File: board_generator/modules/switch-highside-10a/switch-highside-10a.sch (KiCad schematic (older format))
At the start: 7 parts, among them J1 Screw_Terminal_01x01, Q1 NTR5103N, U1 AUIPS7111S, X1 interface, X2 interface

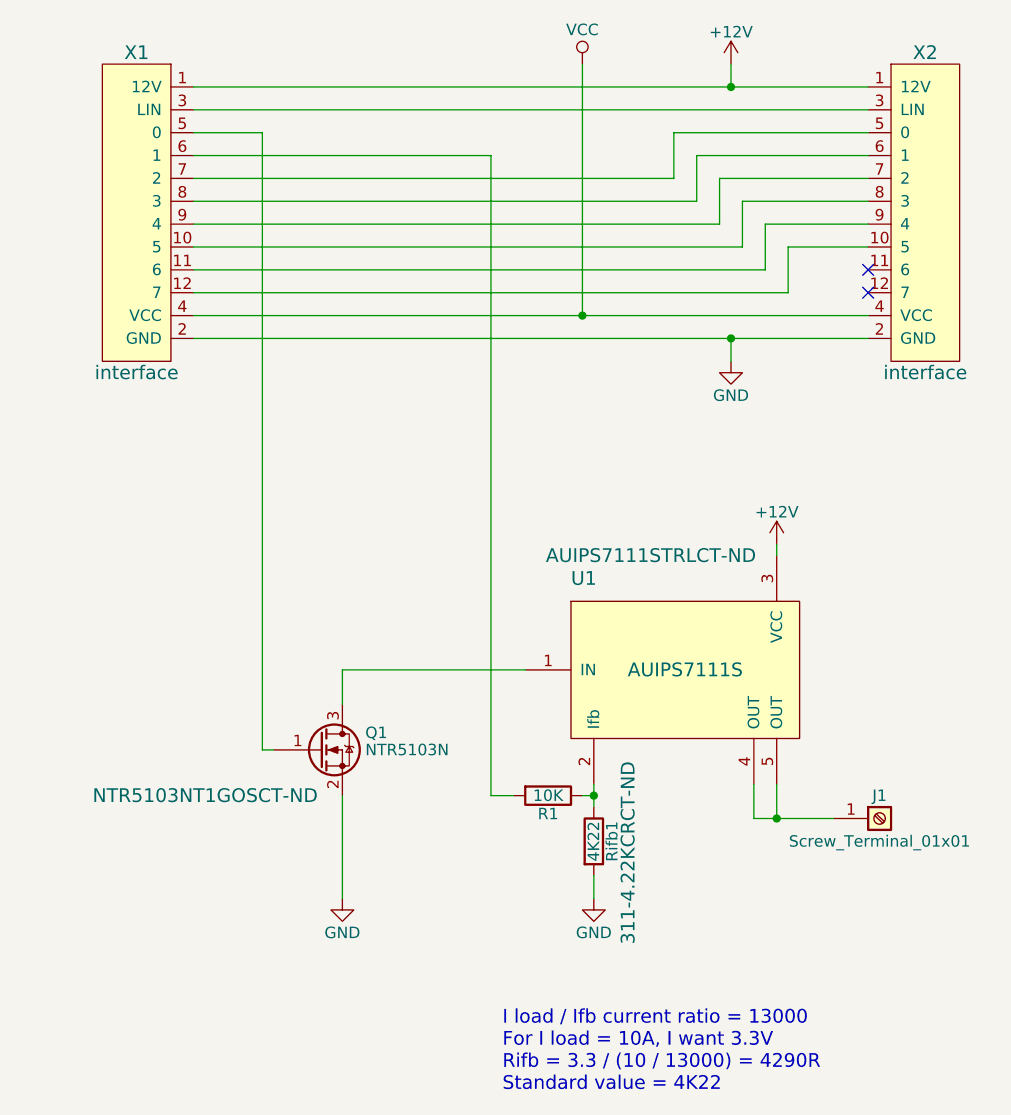
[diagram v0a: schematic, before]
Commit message: Adding pull-down on switch-highside-10a to disable output by default
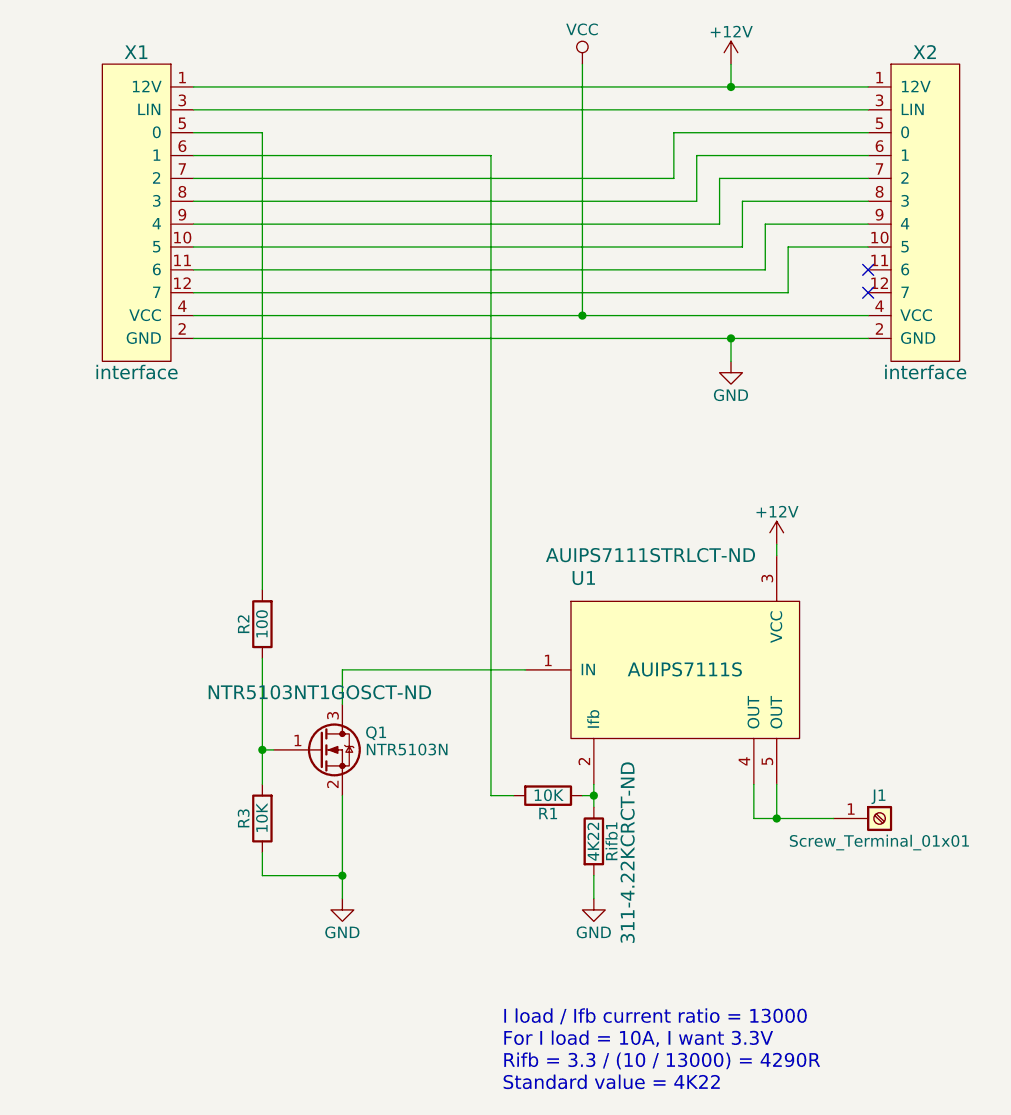
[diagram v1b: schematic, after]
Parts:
- added R2: 100, Resistors_SMD:R_0805_HandSoldering, symbol R
- added R3: 10K, Resistors_SMD:R_0805_HandSoldering, symbol R
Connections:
- net GND: now also R3.1
- net at X1.5 (0): now also R2.2; no longer Q1.1 (G)
- new net: Q1.1 (G), R2.1, R3.2
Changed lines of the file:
@@
 F 2 "TO_SOT_Packages_SMD:SOT-23" H 5200 4475 50  0001 L CIN
 F 3 "NTR5103N-D.PDF" H 5000 4550 50  0001 L CNN
-F 4 "NTR5103NT1GOSCT-ND" H 4500 4350 60  0000 C CNN "DIGIKEY"
+F 4 "NTR5103NT1GOSCT-ND" H 5000 4800 60  0000 C CNN "DIGIKEY"
 	1    5000 4550
 	1    0    0    -1
@@
 	4450 1850 4750 1850
 Wire Wire Line
-	4750 1850 4750 4550
-Wire Wire Line
 	4750 4550 4800 4550
 Text Notes 5800 6050 0    60   ~ 0
 I load / Ifb current ratio = 13000\nFor I load = 10A, I want 3.3V\nRifb = 3.3 / (10 / 13000) = 4290R\nStandard value = 4K22
+$Comp
+L R R3
+U 1 1 5A5EC140
+P 4750 4850
+F 0 "R3" V 4830 4850 50  0000 C CNN
+F 1 "10K" V 4750 4850 50  0000 C CNN
+F 2 "Resistors_SMD:R_0805_HandSoldering" V 4680 4850 50  0001 C CNN
+F 3 "" H 4750 4850 50  0001 C CNN
+F 4 "311-10.0KCRCT-ND" V 4750 4850 60  0001 C CNN "DIGIKEY"
+	1    4750 4850
+	-1   0    0    1
+$EndComp
+Connection ~ 4750 4550
+Wire Wire Line
+	4750 5000 4750 5100
+Wire Wire Line
+	4750 5100 5100 5100
+Connection ~ 5100 5100
+$Comp
+L R R2
+U 1 1 5A5EC27D
+P 4750 4000
+F 0 "R2" V 4830 4000 50  0000 C CNN
+F 1 "100" V 4750 4000 50  0000 C CNN
+F 2 "Resistors_SMD:R_0805_HandSoldering" V 4680 4000 50  0001 C CNN
+F 3 "" H 4750 4000 50  0001 C CNN
+F 4 "311-100CRCT-ND" V 4750 4000 60  0001 C CNN "DIGIKEY"
+	1    4750 4000
+	-1   0    0    1
+$EndComp
+Wire Wire Line
+	4750 4150 4750 4700
+Wire Wire Line
+	4750 1850 4750 3850
 $EndSCHEMATC

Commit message: Adding DigiKey references for switch-highside-10a
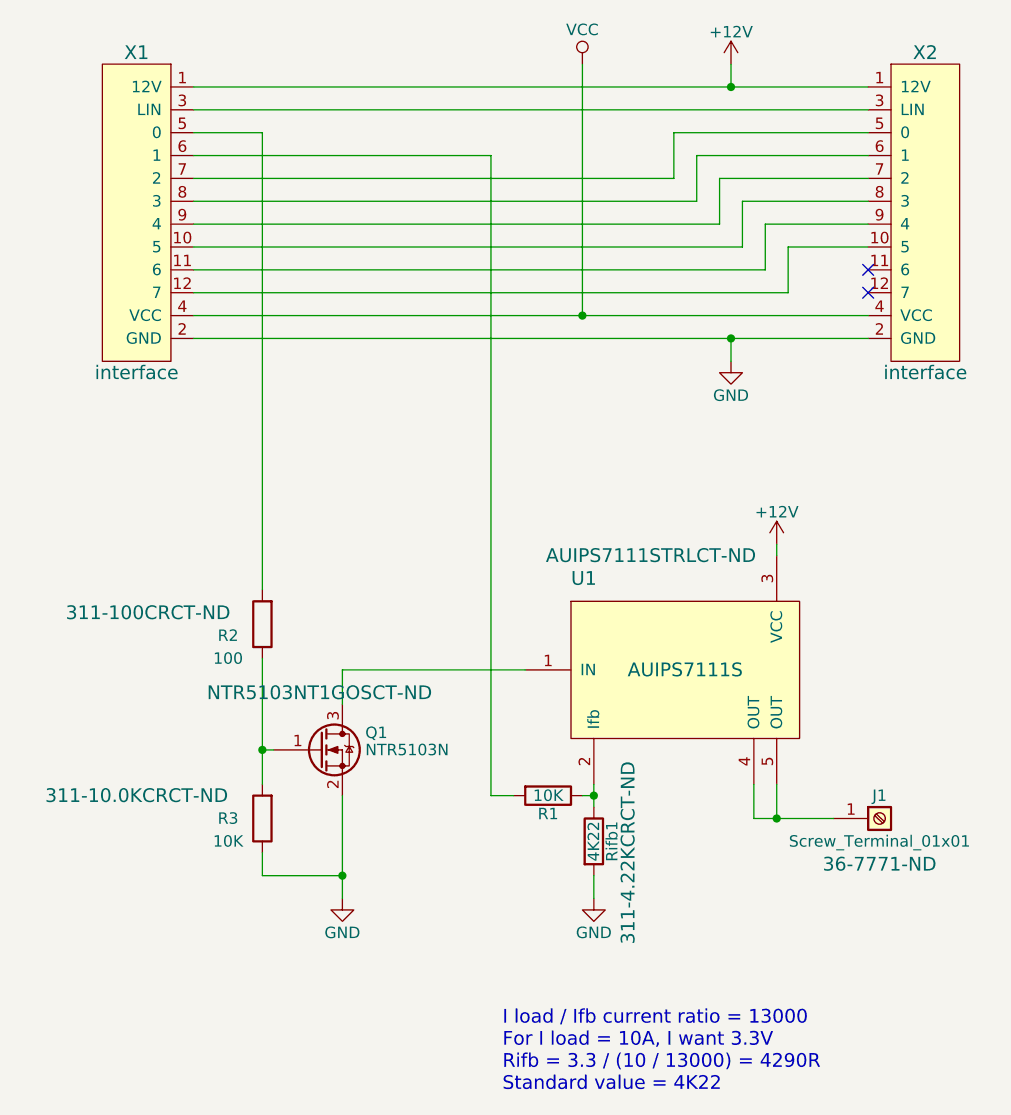
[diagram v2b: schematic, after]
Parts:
- J1: DIGIKEY (none) -> 36-7771-ND
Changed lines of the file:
@@
 F 2 "connectors:TERM_SCREW_M3" H 7450 4850 50  0001 C CNN
 F 3 "" H 7450 4850 50  0001 C CNN
+F 4 "36-7771-ND" H 7450 4650 60  0000 C CNN "DIGIKEY"
 	1    7450 4850
 	1    0    0    -1
@@
 U 1 1 5A5EC140
 P 4750 4850
-F 0 "R3" V 4830 4850 50  0000 C CNN
-F 1 "10K" V 4750 4850 50  0000 C CNN
+F 0 "R3" H 4900 4850 50  0000 C CNN
+F 1 "10K" H 4900 4950 50  0000 C CNN
 F 2 "Resistors_SMD:R_0805_HandSoldering" V 4680 4850 50  0001 C CNN
 F 3 "" H 4750 4850 50  0001 C CNN
-F 4 "311-10.0KCRCT-ND" V 4750 4850 60  0001 C CNN "DIGIKEY"
+F 4 "311-10.0KCRCT-ND" H 5300 4750 60  0000 C CNN "DIGIKEY"
 	1    4750 4850
 	-1   0    0    1
@@
 U 1 1 5A5EC27D
 P 4750 4000
-F 0 "R2" V 4830 4000 50  0000 C CNN
-F 1 "100" V 4750 4000 50  0000 C CNN
+F 0 "R2" H 4900 4050 50  0000 C CNN
+F 1 "100" H 4900 4150 50  0000 C CNN
 F 2 "Resistors_SMD:R_0805_HandSoldering" V 4680 4000 50  0001 C CNN
 F 3 "" H 4750 4000 50  0001 C CNN
-F 4 "311-100CRCT-ND" V 4750 4000 60  0001 C CNN "DIGIKEY"
+F 4 "311-100CRCT-ND" H 5250 3950 60  0000 C CNN "DIGIKEY"
 	1    4750 4000
 	-1   0    0    1
